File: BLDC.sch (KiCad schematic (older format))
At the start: 132 parts, among them J1 43650-0510, J2 436500313, J3 DNP, J4 43650-0510, U1 LMZ21700SIL, U12 MCP9808, U13 AS5047U, U17 INA250, U18 INA250, U19 INA250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

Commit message: WIP adding bonus header to north edge
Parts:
- removed TP1, TP2: TestPoint, TestPoint:TestPoint_Pad_D1.0mm, symbol Connector:TestPoint
- added J5: BONUS, Connector_PinHeader_2.54mm:PinHeader_2x08_P2.54mm_Horizontal, symbol Connector_Generic:Conn_02x08_Odd_Even
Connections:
- net labels added: BONUS0
- wire segments 401 -> 406
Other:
- moved on the sheet: C24, C27
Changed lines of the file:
@@
 L power:+3V3 #PWR039
 U 1 1 5B53BDAA
-P 9900 8050
-F 0 "#PWR039" H 9900 7900 50  0001 C CNN
-F 1 "+3V3" H 9900 8190 50  0000 C CNN
-F 2 "" H 9900 8050 50  0001 C CNN
-F 3 "" H 9900 8050 50  0001 C CNN
-	1    9900 8050
+P 9900 8150
+F 0 "#PWR039" H 9900 8000 50  0001 C CNN
+F 1 "+3V3" H 9900 8290 50  0000 C CNN
+F 2 "" H 9900 8150 50  0001 C CNN
+F 3 "" H 9900 8150 50  0001 C CNN
+	1    9900 8150
 	1    0    0    -1
 $EndComp
@@
 L power:GND #PWR021
 U 1 1 5B530C67
-P 9900 8250
-F 0 "#PWR021" H 9900 8000 50  0001 C CNN
-F 1 "GND" H 9900 8100 50  0001 C CNN
-F 2 "" H 9900 8250 50  0001 C CNN
-F 3 "" H 9900 8250 50  0001 C CNN
-	1    9900 8250
+P 9900 8350
+F 0 "#PWR021" H 9900 8100 50  0001 C CNN
+F 1 "GND" H 9900 8200 50  0001 C CNN
+F 2 "" H 9900 8350 50  0001 C CNN
+F 3 "" H 9900 8350 50  0001 C CNN
+	1    9900 8350
 	1    0    0    -1
 $EndComp
@@
 L Device:C_Small C27
 U 1 1 5B48C437
-P 9900 8150
-F 0 "C27" H 10000 8100 28  0000 L CNN
-F 1 "1u" H 10000 8150 28  0000 L CNN
-F 2 "Capacitor_SMD:C_0402_1005Metric" H 9900 8150 60  0001 C CNN
-F 3 "~" H 9900 8150 60  0001 C CNN
-F 4 "1.0uF" H 9900 8150 60  0001 C CNN "Capacitance"
-F 5 "Digikey" H 10000 8200 50  0001 C CNN "D1N"
-F 6 "490-10017-1-ND " H 10000 8200 50  0001 C CNN "D1PN"
-F 7 "Murata" H 10000 8200 50  0001 C CNN "MFN"
-F 8 "GRM155R61E105KA12D " H 10000 8200 50  0001 C CNN "MPN"
-F 9 "25.0V" H 10000 8200 28  0000 L CNN "Maximum Voltage"
-F 10 "10%" H 9900 8150 60  0001 C CNN "Tolerance"
-	1    9900 8150
+P 9900 8250
+F 0 "C27" H 10000 8200 28  0000 L CNN
+F 1 "1u" H 10000 8250 28  0000 L CNN
+F 2 "Capacitor_SMD:C_0402_1005Metric" H 9900 8250 60  0001 C CNN
+F 3 "~" H 9900 8250 60  0001 C CNN
+F 4 "1.0uF" H 9900 8250 60  0001 C CNN "Capacitance"
+F 5 "Digikey" H 10000 8300 50  0001 C CNN "D1N"
+F 6 "490-10017-1-ND " H 10000 8300 50  0001 C CNN "D1PN"
+F 7 "Murata" H 10000 8300 50  0001 C CNN "MFN"
+F 8 "GRM155R61E105KA12D " H 10000 8300 50  0001 C CNN "MPN"
+F 9 "25.0V" H 10000 8300 28  0000 L CNN "Maximum Voltage"
+F 10 "10%" H 9900 8250 60  0001 C CNN "Tolerance"
+	1    9900 8250
 	-1   0    0    1
 $EndComp
@@
 L Device:C_Small C24
 U 1 1 5B48C431
-P 10250 8150
-F 0 "C24" H 10350 8100 28  0000 L CNN
-F 1 "100n" H 10350 8150 28  0000 L CNN
-F 2 "Capacitor_SMD:C_0402_1005Metric" H 10250 8150 60  0001 C CNN
-F 3 "~" H 10250 8150 60  0001 C CNN
-F 4 "0.1uF" H 10250 8150 60  0001 C CNN "Capacitance"
-F 5 "Digikey" H 10350 8200 50  0001 C CNN "D1N"
-F 6 "1276-1043-1-ND " H 10350 8200 50  0001 C CNN "D1PN"
-F 7 "Samsung" H 10350 8200 50  0001 C CNN "MFN"
-F 8 "CL05A104KA5NNNC " H 10350 8200 50  0001 C CNN "MPN"
-F 9 "25.0V" H 10350 8200 28  0000 L CNN "Maximum Voltage"
-F 10 "10%" H 10250 8150 60  0001 C CNN "Tolerance"
-	1    10250 8150
+P 10250 8250
+F 0 "C24" H 10350 8200 28  0000 L CNN
+F 1 "100n" H 10350 8250 28  0000 L CNN
+F 2 "Capacitor_SMD:C_0402_1005Metric" H 10250 8250 60  0001 C CNN
+F 3 "~" H 10250 8250 60  0001 C CNN
+F 4 "0.1uF" H 10250 8250 60  0001 C CNN "Capacitance"
+F 5 "Digikey" H 10350 8300 50  0001 C CNN "D1N"
+F 6 "1276-1043-1-ND " H 10350 8300 50  0001 C CNN "D1PN"
+F 7 "Samsung" H 10350 8300 50  0001 C CNN "MFN"
+F 8 "CL05A104KA5NNNC " H 10350 8300 50  0001 C CNN "MPN"
+F 9 "25.0V" H 10350 8300 28  0000 L CNN "Maximum Voltage"
+F 10 "10%" H 10250 8250 60  0001 C CNN "Tolerance"
+	1    10250 8250
 	-1   0    0    1
 $EndComp
@@
 Text Label 10350 5750 1    40   ~ 0
 LED_STATUS
-Text Label 2750 9700 2    40   ~ 0
-I2C_SCL
 Text Label 2750 9600 2    40   ~ 0
 I2C_SDA
@@
 	1950 5550 1950 5450
 Wire Wire Line
-	10250 7650 10250 8050
+	10250 7650 10250 8150
 Wire Wire Line
 	1525 3550 1800 3550
@@
 	4850 6150 5250 6150
 Wire Wire Line
-	9900 8250 10250 8250
-Connection ~ 9900 8250
+	9900 8350 10250 8350
+Connection ~ 9900 8350
 Wire Wire Line
-	10250 8050 9900 8050
-Connection ~ 10250 8050
-Connection ~ 9900 8050
+	10250 8150 9900 8150
+Connection ~ 10250 8150
+Connection ~ 9900 8150
 NoConn ~ 10750 7650
 NoConn ~ 10850 7650
@@
 Wire Wire Line
 	10150 5400 10150 5750
-Text Notes 10200 8500 0    50   ~ 0
+Text Notes 10200 8550 0    50   ~ 0
 BOOT0=BOOT1(PB2)=GND\nalways boot from flash
 Text Notes 8250 5150 0    50   ~ 0
 TC2030-MCP-NL
-$Comp
-L Connector:TestPoint TP1
-U 1 1 5D6107FB
-P 2500 9600
-F 0 "TP1" H 2450 9800 50  0000 L CNN
-F 1 "TestPoint" H 2558 9627 50  0001 L CNN
-F 2 "TestPoint:TestPoint_Pad_D1.0mm" H 2700 9600 50  0001 C CNN
-F 3 "~" H 2700 9600 50  0001 C CNN
-	1    2500 9600
-	1    0    0    -1
-$EndComp
 Wire Wire Line
 	3200 1700 2800 1700
@@
 Text Label 3150 1800 2    31   ~ 0
 MOT_PWM_A
-Wire Wire Line
-	2500 9600 2750 9600
-$Comp
-L Connector:TestPoint TP2
-U 1 1 5D6E6BBB
-P 2350 9700
-F 0 "TP2" H 2300 9900 50  0000 L CNN
-F 1 "TestPoint" H 2408 9727 50  0001 L CNN
-F 2 "TestPoint:TestPoint_Pad_D1.0mm" H 2550 9700 50  0001 C CNN
-F 3 "~" H 2550 9700 50  0001 C CNN
-	1    2350 9700
-	1    0    0    -1
-$EndComp
-Wire Wire Line
-	2750 9700 2350 9700
 $Comp
 L Connector:TestPoint TP6
@@
 Text Notes 9750 5200 0    50   ~ 0
 LED_STATUS on\nTIM4_CH3 or\nTIM10_CH1
+$Comp
+L Connector_Generic:Conn_02x08_Odd_Even J5
+U 1 1 5D618427
+P 10300 9700
+F 0 "J5" H 10350 10217 50  0000 C CNN
+F 1 "BONUS" H 10350 10126 50  0000 C CNN
+F 2 "Connector_PinHeader_2.54mm:PinHeader_2x08_P2.54mm_Horizontal" H 10300 9700 50  0001 C CNN
+F 3 "~" H 10300 9700 50  0001 C CNN
+F 4 "DNP" H 10300 9700 50  0001 C CNN "MPN"
+F 5 "DNP" H 10300 9700 50  0001 C CNN "MFN"
+F 6 "DNP" H 10300 9700 50  0001 C CNN "D1PN"
+F 7 "DNP" H 10300 9700 50  0001 C CNN "D1N"
+	1    10300 9700
+	1    0    0    -1
+$EndComp
+$Comp
+L power:+3V3 #PWR0130
+U 1 1 5D66891E
+P 10750 10250
+F 0 "#PWR0130" H 10750 10100 50  0001 C CNN
+F 1 "+3V3" H 10750 10390 50  0000 C CNN
+F 2 "" H 10750 10250 50  0001 C CNN
+F 3 "" H 10750 10250 50  0001 C CNN
+	1    10750 10250
+	1    0    0    -1
+$EndComp
+Wire Wire Line
+	10600 10100 10600 10250
+Wire Wire Line
+	10600 10250 10750 10250
+Wire Wire Line
+	9950 10250 10100 10250
+Wire Wire Line
+	10100 10250 10100 10100
+$Comp
+L power:GND #PWR0133
+U 1 1 5D66B594
+P 10950 10000
+F 0 "#PWR0133" H 10950 9750 50  0001 C CNN
+F 1 "GND" H 10950 9850 50  0001 C CNN
+F 2 "" H 10950 10000 50  0001 C CNN
+F 3 "" H 10950 10000 50  0001 C CNN
+	1    10950 10000
+	1    0    0    -1
+$EndComp
+Wire Wire Line
+	10600 10000 10950 10000
+$Comp
+L power:GND #PWR0134
+U 1 1 5D66B98C
+P 10950 9300
+F 0 "#PWR0134" H 10950 9050 50  0001 C CNN
+F 1 "GND" H 10950 9150 50  0001 C CNN
+F 2 "" H 10950 9300 50  0001 C CNN
+F 3 "" H 10950 9300 50  0001 C CNN
+	1    10950 9300
+	1    0    0    -1
+$EndComp
+Wire Wire Line
+	10950 9300 10600 9300
+Wire Wire Line
+	10600 9300 10600 9400
+Text Label 10050 7650 3    50   ~ 0
+BONUS0
+Text Label 10100 9400 2    50   ~ 0
+BONUS0
+$Comp
+L power:+3V3 #PWR0131
+U 1 1 5D725A15
+P 9950 10250
+F 0 "#PWR0131" H 9950 10100 50  0001 C CNN
+F 1 "+3V3" H 9950 10390 50  0000 C CNN
+F 2 "" H 9950 10250 50  0001 C CNN
+F 3 "" H 9950 10250 50  0001 C CNN
+	1    9950 10250
+	1    0    0    -1
+$EndComp
+Text Label 10100 10000 2    40   ~ 0
+I2C_SCL
+Text Label 10100 9900 2    40   ~ 0
+I2C_SDA
+Text Label 2750 9700 2    40   ~ 0
+I2C_SCL
 $EndSCHEMATC

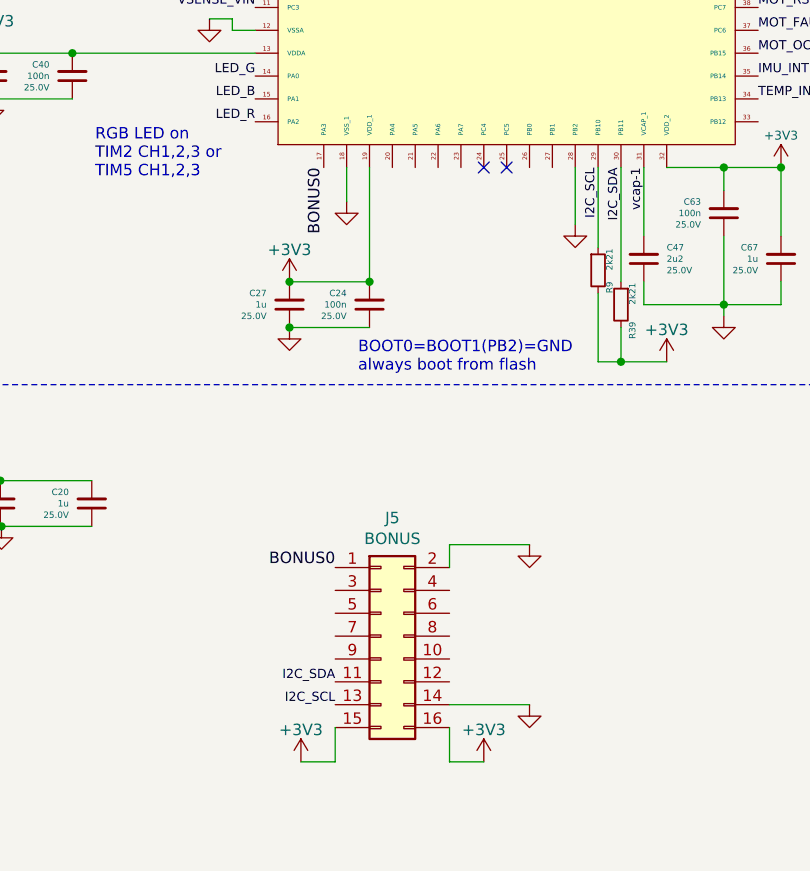
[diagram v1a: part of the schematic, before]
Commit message: finish up bonus connector
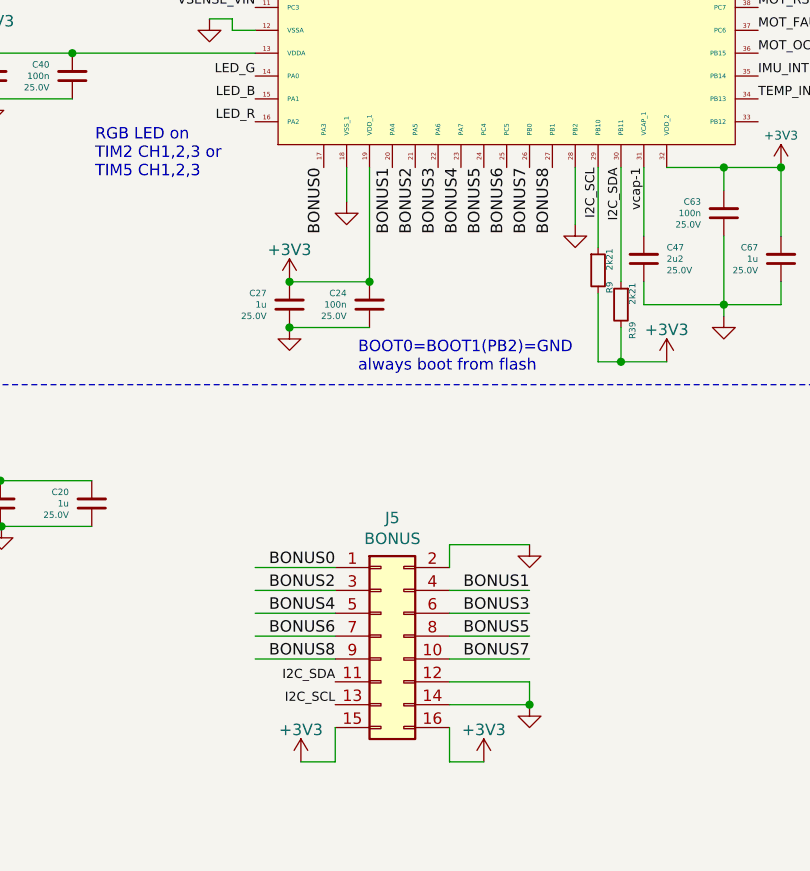
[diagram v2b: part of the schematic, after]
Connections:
- net labels added: BONUS1, BONUS2, BONUS3, BONUS4, BONUS5, BONUS6, BONUS7, BONUS8
- wire segments 406 -> 417
- no-connect marks 22 -> 20
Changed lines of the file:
@@
 Connection ~ 10250 8150
 Connection ~ 9900 8150
-NoConn ~ 10750 7650
-NoConn ~ 10850 7650
 Text Notes 9050 7700 0    50   ~ 0
 RGB LED on\nTIM2 CH1,2,3 or\nTIM5 CH1,2,3
@@
 Text Label 2750 9700 2    40   ~ 0
 I2C_SCL
+Text Label 10350 7650 3    50   ~ 0
+BONUS1
+Text Label 10450 7650 3    50   ~ 0
+BONUS2
+Text Label 10550 7650 3    50   ~ 0
+BONUS3
+Text Label 10650 7650 3    50   ~ 0
+BONUS4
+Text Label 10750 7650 3    50   ~ 0
+BONUS5
+Text Label 10850 7650 3    50   ~ 0
+BONUS6
+Text Label 10950 7650 3    50   ~ 0
+BONUS7
+Text Label 11050 7650 3    50   ~ 0
+BONUS8
+Text Label 10950 9500 2    50   ~ 0
+BONUS1
+Wire Wire Line
+	10600 9500 10950 9500
+Wire Wire Line
+	10100 9400 9750 9400
+Wire Wire Line
+	9750 9500 10100 9500
+Text Label 10100 9500 2    50   ~ 0
+BONUS2
+Wire Wire Line
+	10600 9600 10950 9600
+Text Label 10950 9600 2    50   ~ 0
+BONUS3
+Text Label 10100 9600 2    50   ~ 0
+BONUS4
+Wire Wire Line
+	9750 9600 10100 9600
+Text Label 10950 9700 2    50   ~ 0
+BONUS5
+Wire Wire Line
+	10600 9700 10950 9700
+Wire Wire Line
+	9750 9700 10100 9700
+Text Label 10100 9700 2    50   ~ 0
+BONUS6
+Wire Wire Line
+	10600 9800 10950 9800
+Text Label 10950 9800 2    50   ~ 0
+BONUS7
+Wire Wire Line
+	9750 9800 10100 9800
+Text Label 10100 9800 2    50   ~ 0
+BONUS8
+Wire Wire Line
+	10600 9900 10950 9900
+Wire Wire Line
+	10950 9900 10950 10000
+Connection ~ 10950 10000
 $EndSCHEMATC

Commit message: a bit more pcb cleanup, add slow-start cap MPN and gerbv project
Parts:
- C34: value 3n3 -> 4n7; Capacitance 3n3 -> 4n7; D1PN TBD -> 311-1039-1-ND; MFN TBD -> Yageo; MPN TBD -> CC0402KRX7R8BB472
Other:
- note added: "2.35ms\nsoft-start time"
- note removed: "1.1ms\nsoft-start time\nto share 2n2 cap with\n12v BOM line item"
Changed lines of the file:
@@
 P 7375 1900
 F 0 "C34" H 7475 1850 28  0000 L CNN
-F 1 "3n3" H 7475 1900 28  0000 L CNN
+F 1 "4n7" H 7475 1900 28  0000 L CNN
 F 2 "Capacitor_SMD:C_0402_1005Metric" H 7375 1900 60  0001 C CNN
 F 3 "~" H 7375 1900 60  0001 C CNN
-F 4 "3n3" H 7375 1900 60  0001 C CNN "Capacitance"
+F 4 "4n7" H 7375 1900 60  0001 C CNN "Capacitance"
 F 5 "Digikey" H 7475 1950 50  0001 C CNN "D1N"
-F 6 "TBD" H 7475 1950 50  0001 C CNN "D1PN"
-F 7 "TBD" H 7475 1950 50  0001 C CNN "MFN"
-F 8 "TBD" H 7475 1950 50  0001 C CNN "MPN"
+F 6 "311-1039-1-ND" H 7475 1950 50  0001 C CNN "D1PN"
+F 7 "Yageo" H 7475 1950 50  0001 C CNN "MFN"
+F 8 "CC0402KRX7R8BB472" H 7475 1950 50  0001 C CNN "MPN"
 F 9 "25V" H 7475 1950 28  0000 L CNN "Maximum Voltage"
 F 10 "10%" H 7375 1900 60  0001 C CNN "Tolerance"
@@
 Text Notes 5750 2225 0    79   ~ 16
 snubber
-Text Notes 6850 2500 0    50   ~ 0
-1.1ms\nsoft-start time\nto share 2n2 cap with\n12v BOM line item
+Text Notes 6950 2350 0    50   ~ 0
+2.35ms\nsoft-start time
 Text Notes 1500 2325 0    50   ~ 0
 top-side ceramics

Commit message: update BOM file
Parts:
- C12, C31: Capacitance 22uF -> 22u
- C35: Capacitance 22.0uF -> 22u
- C41: Capacitance 47.0uF -> 22u
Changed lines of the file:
@@
 F 2 "Capacitor_SMD:C_1210_3225Metric" H 10040 1750 60  0001 C CNN
 F 3 "~" H 10040 1750 60  0001 C CNN
-F 4 "22.0uF" H 10040 1750 60  0001 C CNN "Capacitance"
+F 4 "22u" H 10040 1750 60  0001 C CNN "Capacitance"
 F 5 "Digikey" H 10140 1800 50  0001 C CNN "D1N"
 F 6 "1276-1101-1-ND" H 10140 1800 50  0001 C CNN "D1PN"
@@
 F 2 "Capacitor_SMD:C_1210_3225Metric" H 10275 3625 60  0001 C CNN
 F 3 "~" H 10275 3625 60  0001 C CNN
-F 4 "22uF" H 10275 3625 60  0001 C CNN "Capacitance"
+F 4 "22u" H 10275 3625 60  0001 C CNN "Capacitance"
 F 5 "Digikey" H 10375 3775 50  0001 C CNN "D1N"
 F 6 "1276-1101-1-ND" H 10375 3775 50  0001 C CNN "D1PN"
@@
 F 2 "Capacitor_SMD:C_1210_3225Metric" H 7075 1600 60  0001 C CNN
 F 3 "~" H 7075 1600 60  0001 C CNN
-F 4 "22uF" H 7075 1600 60  0001 C CNN "Capacitance"
+F 4 "22u" H 7075 1600 60  0001 C CNN "Capacitance"
 F 5 "Digikey" H 7175 1650 50  0001 C CNN "D1N"
 F 6 "1276-1101-1-ND" H 7175 1650 50  0001 C CNN "D1PN"
@@
 F 2 "Capacitor_SMD:C_1210_3225Metric" H 8700 1750 60  0001 C CNN
 F 3 "~" H 8700 1750 60  0001 C CNN
-F 4 "47.0uF" H 8700 1750 60  0001 C CNN "Capacitance"
+F 4 "22u" H 8700 1750 60  0001 C CNN "Capacitance"
 F 5 "Digikey" H 8800 1800 50  0001 C CNN "D1N"
 F 6 "1276-1101-1-ND" H 8800 1800 50  0001 C CNN "D1PN"

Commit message: WIP new revision, change INA250 to INA253 (higher bandwidth), regulator to low EMI version
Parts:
- removed C28, C29: DNP, Capacitor_SMD:C_0603_1608Metric, symbol Device:C_Small
- removed C33: 1u, Capacitor_SMD:C_0402_1005Metric, symbol Device:C_Small
- removed R1: 40k2, Resistor_SMD:R_0805_2012Metric, symbol Device:R_Small
- removed R12, R13, R14: DNP, Resistor_SMD:R_0805_2012Metric, symbol Device:R_Small
- removed R7: 255k, Resistor_SMD:R_0603_1608Metric, symbol Device:R_Small
- removed U17, U18, U19: INA250, Package_SO:TSSOP-16_4.4x5mm_P0.65mm, symbol BLDC:INA250
- removed U4: LM5163, Package_SO:SOIC-8-1EP_3.9x4.9mm_P1.27mm_EP2.41x3.3mm, symbol BLDC:ti-LM5163
- removed U8: REF3312AIDBZ, Package_TO_SOT_SMD:SOT-23, symbol Reference_Voltage:REF3012
- added U10, U11, U14: INA253, Package_SO:TSSOP-20_4.4x6.5mm_P0.65mm, symbol BLDC:INA253
- added U4: LM46000, BLDC:PWP0016G, symbol BLDC:LM46000
- C10: value 47p -> 2u2; footprint Capacitor_SMD:C_0402_1005Metric -> Capacitor_SMD:C_0805_2012Metric; Capacitance 47pF -> 2.2uF; D1PN 490-10683-1-ND -> CHANGEME; MPN GRM1555C1E470JA01D -> CHANGEME; Maximum Voltage 50V -> 25V
- C11: value 2n2 -> 82p; footprint Capacitor_SMD:C_0805_2012Metric -> Capacitor_SMD:C_0402_1005Metric; Capacitance 2.2nF -> 82pF; D1PN 1276-1825-1-ND -> CHANGEME
- C17: value 2n2 -> 470n; footprint Capacitor_SMD:C_0805_2012Metric -> Capacitor_SMD:C_0402_1005Metric; Capacitance 2.2nF -> 470nF; D1PN 1276-1825-1-ND -> CHANGEME; Maximum Voltage 50V -> 6.3V
- C23: value DNP -> 22u; footprint Capacitor_SMD:C_0603_1608Metric -> Capacitor_SMD:C_1210_3225Metric; Capacitance (none) -> 22u; D1N DNP -> Digikey; D1PN DNP -> 1276-1101-1-ND; MFN DNP -> Samsung; MPN DNP -> CL32A226KAJNNNE; Maximum Voltage (none) -> 25V; Tolerance (none) -> 10%
- C7: value 100n -> 4u7; footprint Capacitor_SMD:C_0402_1005Metric -> Capacitor_SMD:C_1210_3225Metric; Capacitance 0.1uF -> 4.7uF; D1PN 1276-1043-1-ND -> 1276-7060-1-ND; MPN CL05A104KA5NNNC -> CL32B475KCVZW6E; Maximum Voltage 25.0V -> 100V
- C8: value 1u -> 4u7; footprint Capacitor_SMD:C_0402_1005Metric -> Capacitor_SMD:C_0805_2012Metric; Capacitance 1.0uF -> 4.7uF; D1PN 490-10017-1-ND -> CHANGEME; MPN GRM155R61E105KA12D -> CHANGEME; Maximum Voltage 25.0V -> 25V; Tolerance 10% -> 5%
- J2: footprint BLDC:molex-microfit-3-pkg_242 -> BLDC:molex-microfit-3-pkg
- L2: value 82u -> 100u; Inductance 82.0uH -> 100.0uH; MPN DR74-820-R -> CHANGEME
- R11: value 49k9 -> 92k; D1PN P49.9KHCT-ND -> CHANGEME
- R8: value 453k -> 1M; D1PN 311-453KHRCT-ND -> CHANGEME
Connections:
- net labels added: motor_phase-A, motor_phase-B, motor_phase-C
- net labels removed: +1V2, GND_A, GND_B, GND_C
- wire segments 417 -> 407
- no-connect marks 20 -> 22
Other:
- note added: "TODO check input / output caps"
- note removed: "746 kHz to allow smaller inductor"
- note removed: "snubber"
- moved on the sheet: C10, C11, C12, C13, C14, C16, C17, C45, L2, R11, R8, TP10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

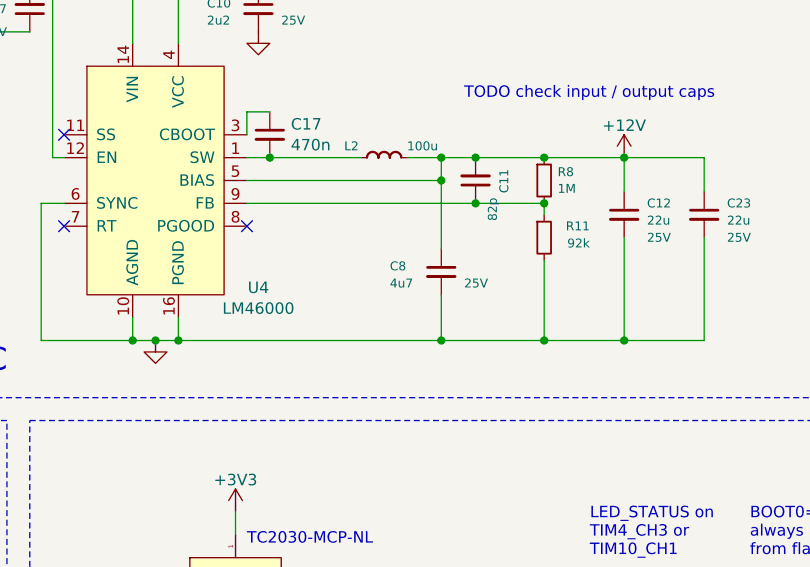
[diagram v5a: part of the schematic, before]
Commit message: tinker with layout, mostly with 12v dc-dc
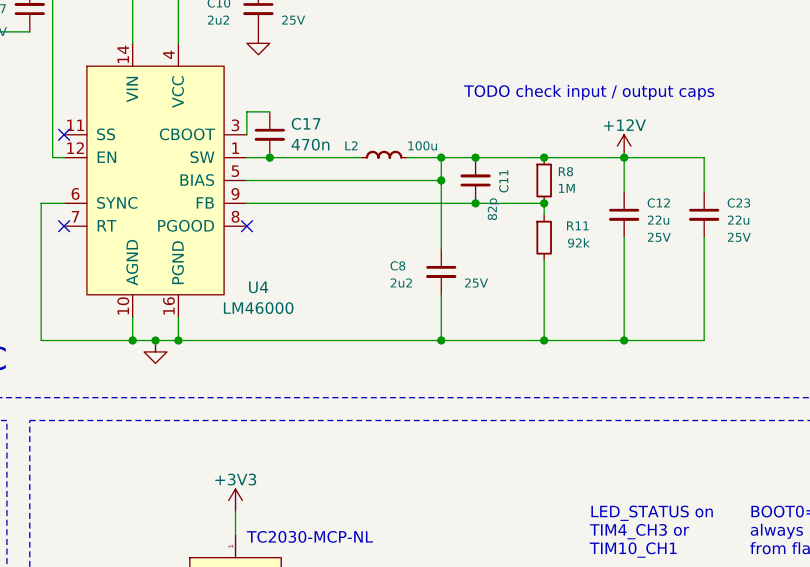
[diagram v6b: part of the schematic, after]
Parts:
- C10: footprint Capacitor_SMD:C_0805_2012Metric -> Capacitor_SMD:C_0603_1608Metric
- C8: value 4u7 -> 2u2; footprint Capacitor_SMD:C_0805_2012Metric -> Capacitor_SMD:C_0603_1608Metric; Capacitance 4.7uF -> 2.2uF
- R11, R8: footprint Resistor_SMD:R_0603_1608Metric -> Resistor_SMD:R_0402_1005Metric
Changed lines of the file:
@@
 Wire Wire Line
 	8350 3250 8250 3250
-$Comp
-L Device:C_Small C8
-U 1 1 5D9DEFCF
-P 9100 3950
-F 0 "C8" H 8875 3975 39  0000 L CNN
-F 1 "4u7" H 8875 3900 39  0000 L CNN
-F 2 "Capacitor_SMD:C_0805_2012Metric" H 9100 3950 60  0001 C CNN
-F 3 "~" H 9100 3950 60  0001 C CNN
-F 4 "4.7uF" H 9100 3950 60  0001 C CNN "Capacitance"
-F 5 "Digikey" H 8875 4075 50  0001 C CNN "D1N"
-F 6 "CHANGEME" H 8875 4075 50  0001 C CNN "D1PN"
-F 7 "Murata" H 8875 4075 50  0001 C CNN "MFN"
-F 8 "CHANGEME" H 8875 4075 50  0001 C CNN "MPN"
-F 9 "25V" H 9200 3900 39  0000 L CNN "Maximum Voltage"
-F 10 "5%" H 9100 3950 60  0001 C CNN "Tolerance"
-	1    9100 3950
-	1    0    0    -1
-$EndComp
 Wire Wire Line
 	7950 4250 7850 4250
@@
 F 0 "C10" H 8075 2825 39  0000 L CNN
 F 1 "2u2" H 8075 2750 39  0000 L CNN
-F 2 "Capacitor_SMD:C_0805_2012Metric" H 8300 2800 60  0001 C CNN
+F 2 "Capacitor_SMD:C_0603_1608Metric" H 8300 2800 60  0001 C CNN
 F 3 "~" H 8300 2800 60  0001 C CNN
 F 4 "2.2uF" H 8300 2800 60  0001 C CNN "Capacitance"
@@
 F 0 "R11" H 9750 3850 39  0000 R CNN
 F 1 "92k" H 9750 3775 39  0000 R CNN
-F 2 "Resistor_SMD:R_0603_1608Metric" H 9550 3800 50  0001 C CNN
+F 2 "Resistor_SMD:R_0402_1005Metric" H 9550 3800 50  0001 C CNN
 F 3 "~" H 9550 3800 50  0001 C CNN
 F 4 "Digikey" H 9692 3937 50  0001 C CNN "D1N"
@@
 F 0 "R8" H 9609 3587 39  0000 L CNN
 F 1 "1M" H 9609 3514 39  0000 L CNN
-F 2 "Resistor_SMD:R_0603_1608Metric" H 9550 3550 50  0001 C CNN
+F 2 "Resistor_SMD:R_0402_1005Metric" H 9550 3550 50  0001 C CNN
 F 3 "~" H 9550 3550 50  0001 C CNN
 F 4 "Digikey" H 9609 3687 50  0001 C CNN "D1N"
@@
 Text Notes 9200 3200 0    50   ~ 0
 TODO check input / output caps
+$Comp
+L Device:C_Small C8
+U 1 1 5D99793A
+P 9100 3950
+F 0 "C8" H 8875 3975 39  0000 L CNN
+F 1 "2u2" H 8875 3900 39  0000 L CNN
+F 2 "Capacitor_SMD:C_0603_1608Metric" H 9100 3950 60  0001 C CNN
+F 3 "~" H 9100 3950 60  0001 C CNN
+F 4 "2.2uF" H 9100 3950 60  0001 C CNN "Capacitance"
+F 5 "Digikey" H 8875 4075 50  0001 C CNN "D1N"
+F 6 "CHANGEME" H 8875 4075 50  0001 C CNN "D1PN"
+F 7 "Murata" H 8875 4075 50  0001 C CNN "MFN"
+F 8 "CHANGEME" H 8875 4075 50  0001 C CNN "MPN"
+F 9 "25V" H 9200 3900 39  0000 L CNN "Maximum Voltage"
+F 10 "5%" H 9100 3950 60  0001 C CNN "Tolerance"
+	1    9100 3950
+	1    0    0    -1
+$EndComp
 $EndSCHEMATC
